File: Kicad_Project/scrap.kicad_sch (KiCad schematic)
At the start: 232 parts, among them J1 Conn_01x07, J2 Conn_01x06, J3 Conn_01x06, J4 Conn_01x06, U1 TF2190-TAH, U2 TF2190-TAH, U3 TF2190-TAH, U4 NCS20034DR2G, U5 STM32F405_pill, U6 PQDE6W-Q110 / RD5-110S12W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

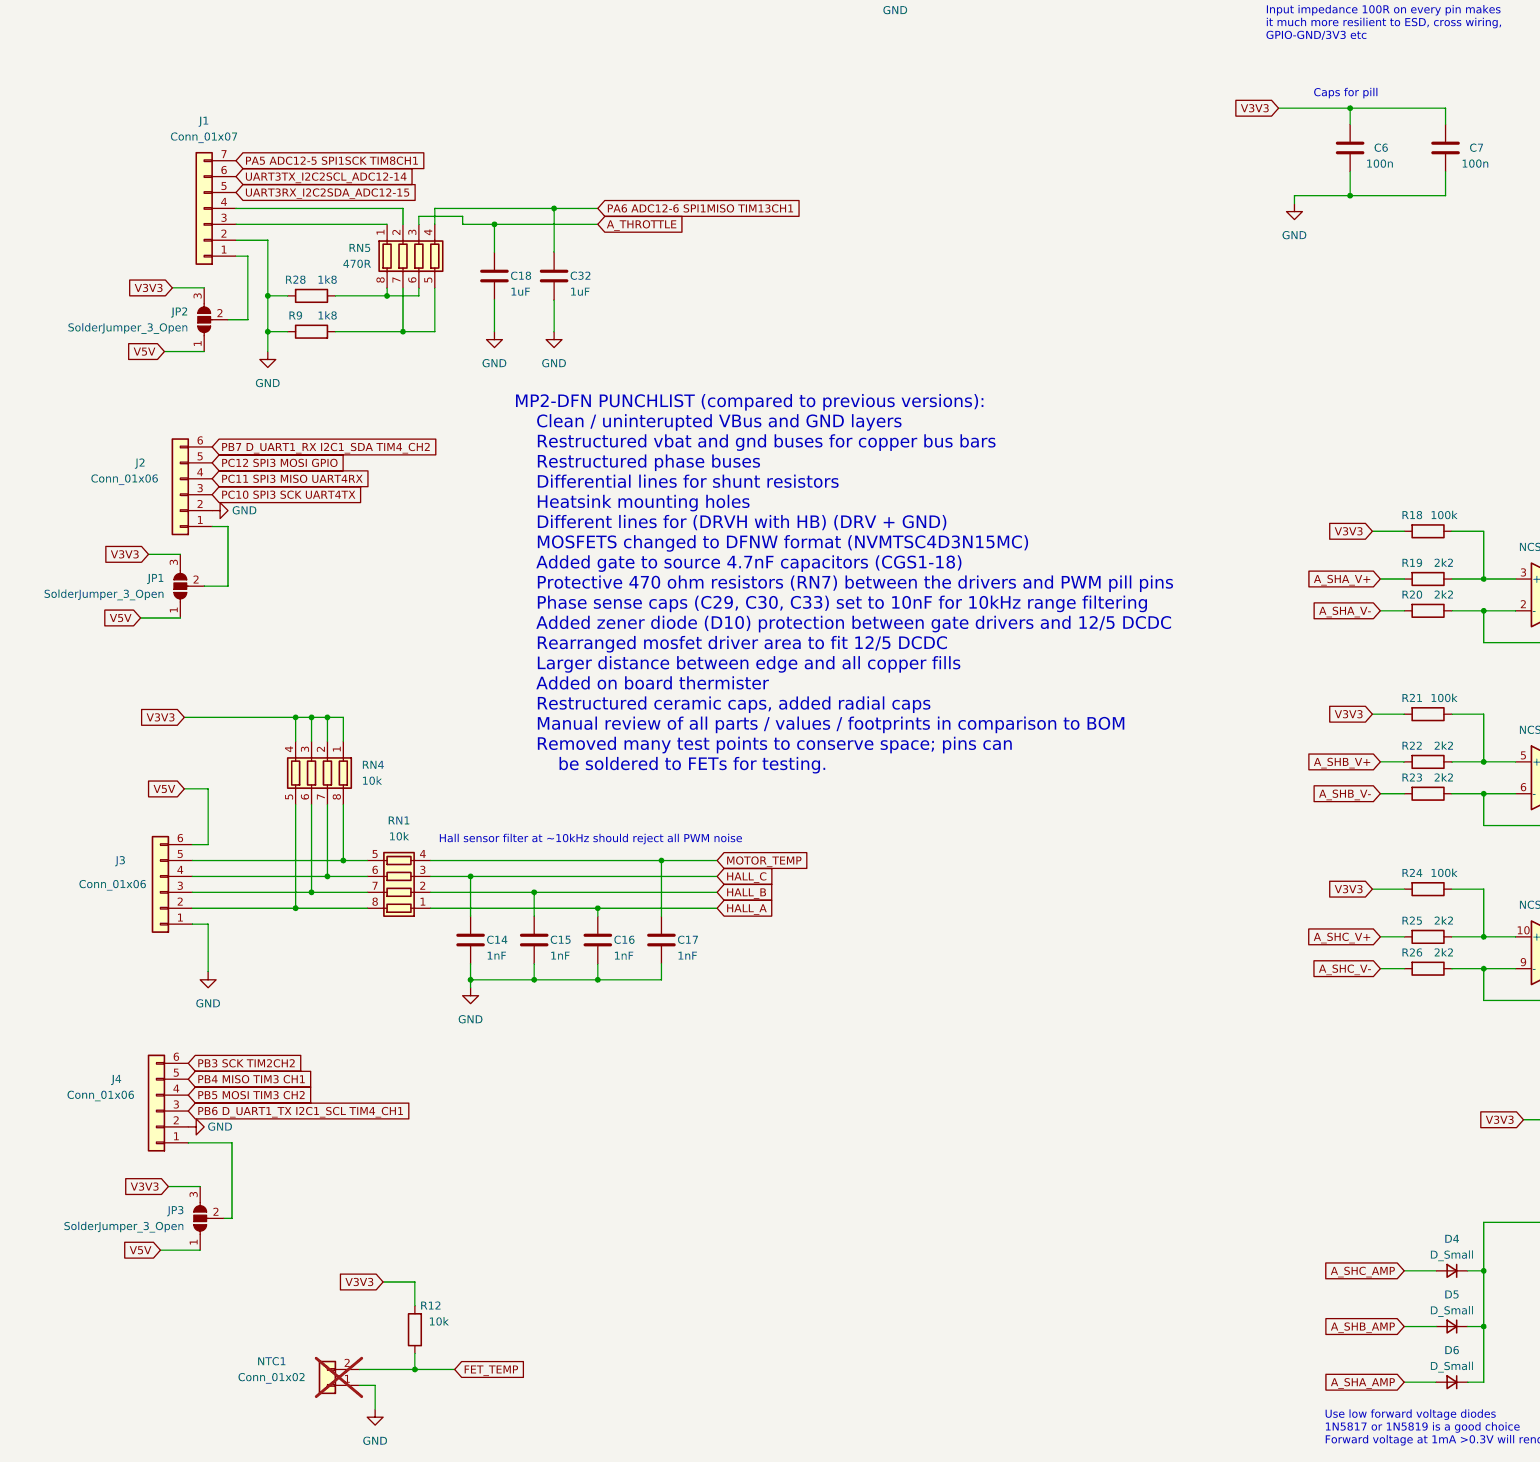
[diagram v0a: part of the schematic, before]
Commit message: minor revision to extend VBAT terminals
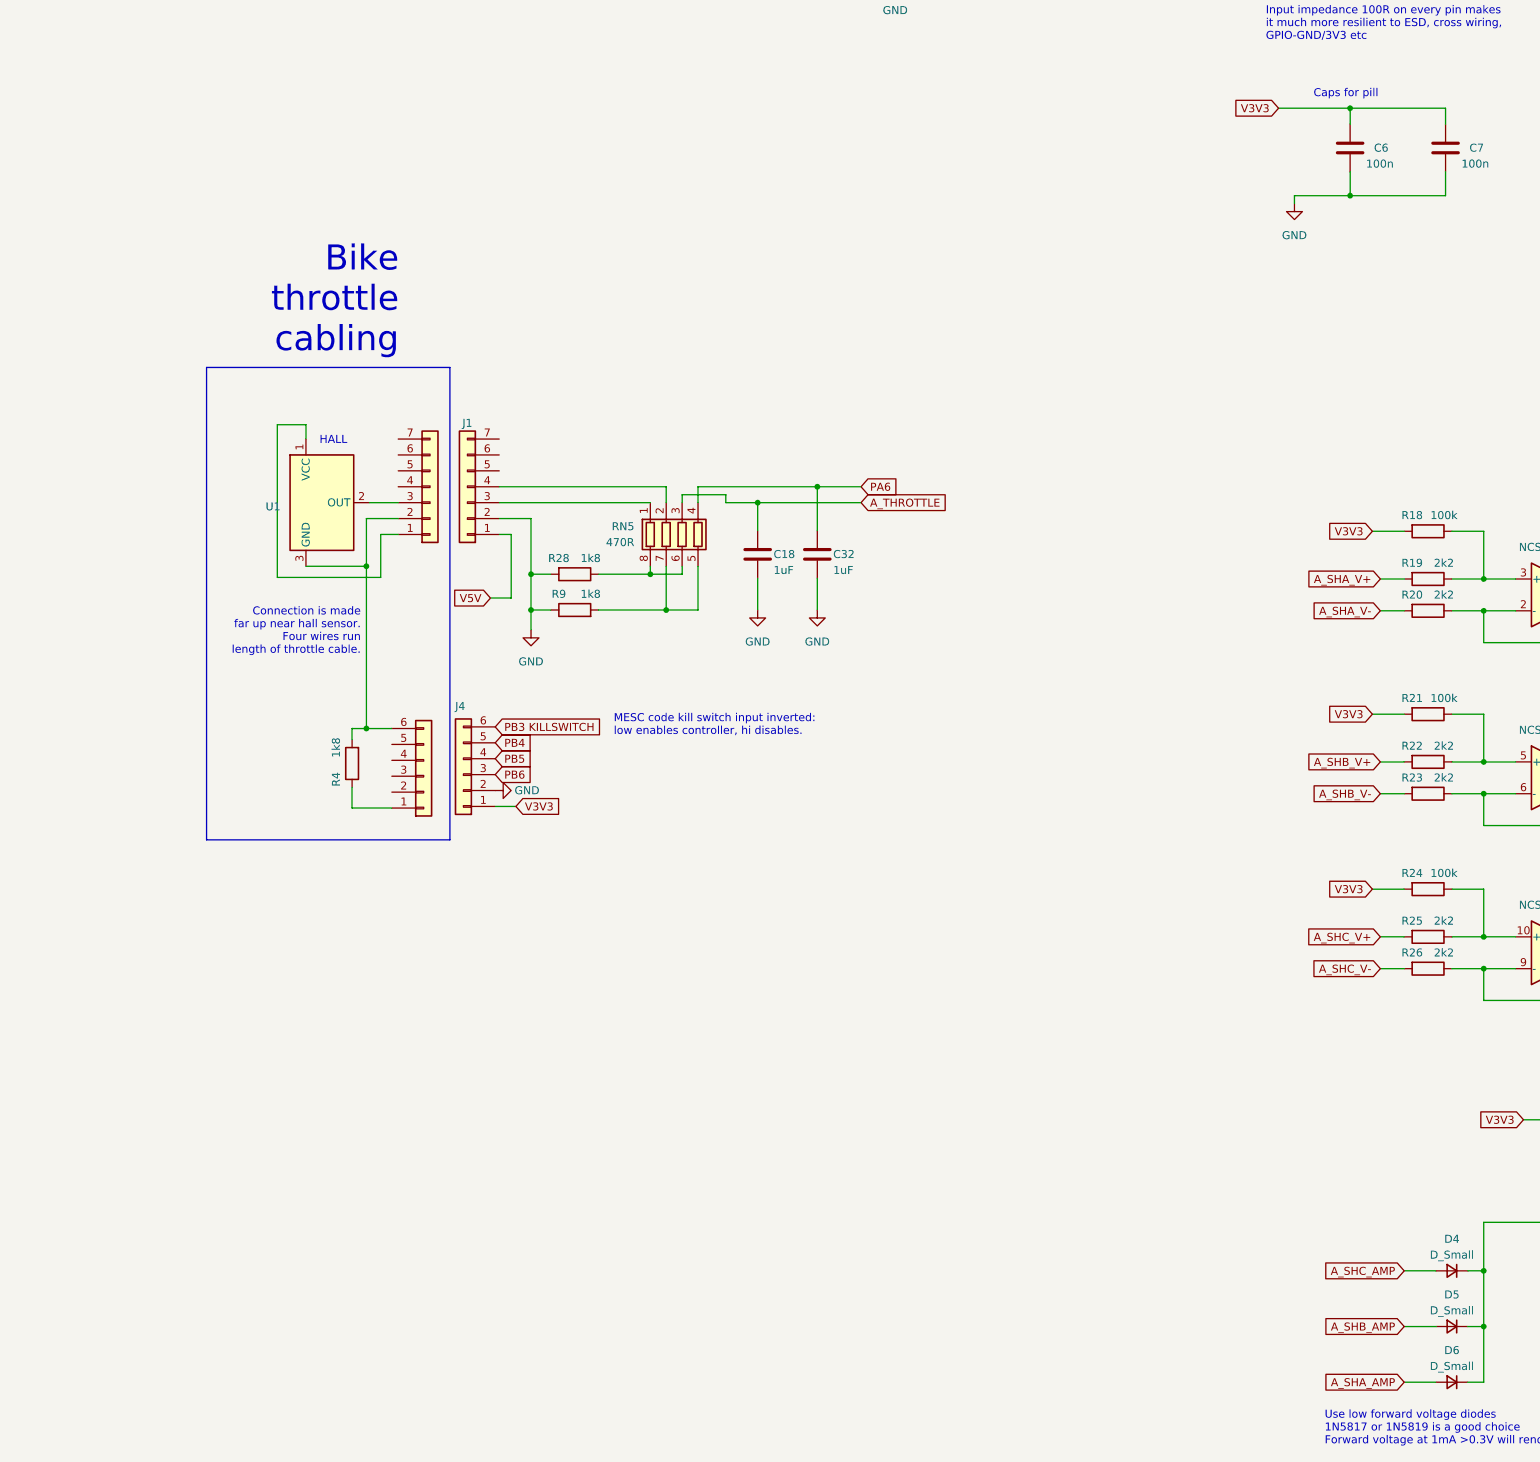
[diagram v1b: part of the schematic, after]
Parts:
- removed C14, C15, C16, C17: 1nF, Capacitor_SMD:C_0603_1608Metric, symbol Device:C
- removed J3: Conn_01x06, Connector_JST:JST_PH_B6B-PH-K_1x06_P2.00mm_Vertical, symbol Connector_Generic:Conn_01x06
- removed JP1, JP2, JP3: SolderJumper_3_Open, Jumper:SolderJumper-3_P1.3mm_Open_RoundedPad1.0x1.5mm_NumberLabels, symbol Jumper:SolderJumper_3_Open
- removed NTC1: Conn_01x02, Resistor_THT:R_Axial_DIN0204_L3.6mm_D1.6mm_P1.90mm_Vertical, symbol Connector_Generic:Conn_01x02
- removed R12: 10k, Resistor_SMD:R_0603_1608Metric, symbol Device:R
- removed RN1, RN4: 10k, Resistor_SMD:R_Array_Concave_4x0603, symbol Device:R_Pack04
- added J3: Conn_01x07, Connector_JST:JST_PH_B7B-PH-K_1x07_P2.00mm_Vertical, symbol Connector_Generic:Conn_01x07
- added R4: 1k8, Resistor_SMD:R_0603_1608Metric, symbol Device:R
- added U1: DRV5055A3xDBZxQ1, Package_TO_SOT_SMD:SOT-23, symbol Sensor_Magnetic:DRV5055A3xDBZxQ1
- D9: LCSC C375575 -> C72041
- SHA1, SHA2, SHA3, SHB1, SHB2, SHB3, SHC1, SHC2, SHC3: LCSC C500733 -> C710260
- TH1: LCSC C222491 -> C531304
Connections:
- net GND: no longer J2.2 (Pin_2)
- net PA5 ADC12-5 SPI1SCK TIM8CH1: no longer J1.7 (Pin_7)
- net PA6 ADC12-6 SPI1MISO TIM13CH1: no longer C32.1, RN5.4 (R4.1)
- net PB3 SCK TIM2CH2: no longer J4.6 (Pin_6)
- net PB4 MISO TIM3 CH1: no longer J4.5 (Pin_5)
- net PB5 MOSI TIM3 CH2: no longer J4.4 (Pin_4)
- net PB6 D_UART1_TX I2C1_SCL TIM4_CH1: no longer J4.3 (Pin_3)
- net PB7 D_UART1_RX I2C1_SDA TIM4_CH2: no longer J2.6 (Pin_6)
- net PC10 SPI3 SCK UART4TX: no longer J2.3 (Pin_3)
- net PC11 SPI3 MISO UART4RX: no longer J2.4 (Pin_4)
- net PC12 SPI3 MOSI GPIO: no longer J2.5 (Pin_5)
- net UART3RX_I2C2SDA_ADC12-15: no longer J1.5 (Pin_5)
- net UART3TX_I2C2SCL_ADC12-14: no longer J1.6 (Pin_6)
- net V3V3: now also J4.1 (Pin_1)
- net at J2.1 (Pin_1): now also R4.1
- new net: J3.1 (Pin_1), U1.1 (VCC)
- new net: J2.6 (Pin_6), J3.2 (Pin_2), R4.2, U1.3 (GND)
- new net: J3.3 (Pin_3), U1.2 (OUT)
- new net PA6: C32.1, RN5.4 (R4.1)
- new net PB3 KILLSWITCH: J4.6 (Pin_6)
- new net PB4: J4.5 (Pin_5)
- new net PB5: J4.4 (Pin_4)
- new net PB6: J4.3 (Pin_3)
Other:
- note added: "Bike throttle cabling"
- note added: "Connection is made far up near hall sensor. Four wires run length of throttle cable."
- note added: "HALL"
- note added: "MESC code kill switch input inverted: low enables controller, hi disables."
- note removed: "Hall sensor filter at ~10kHz should reject all PWM noise"
- note removed: "MP2-DFN PUNCHLIST (compared to previous versions): Clean / uninterupted VBus and GND layers Restructured vbat and gnd buses for copper bus bars Restructured phase buses Differential lines for shunt resistors Heatsink mounting holes Different lines for (DRVH with HB) (DRV + GND) MOSFETS changed to DFNW format (NVMTSC4D3N15MC) Added gate to source 4.7nF capacitors (CGS1-18) Protective 470 ohm resis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"
- moved on the sheet: C18, C32, J1, J4, R28, R9, RN5
